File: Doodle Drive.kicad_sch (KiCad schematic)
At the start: 37 parts, among them J1 USB_B, J2 PINHD_1x4_Male, J6 PINHD_1x2_Male, SW1 Push_Button, SW2 Push_Button, SW3 Push_Button, U1 STM32F411RETx, U6 AP7343-30W5-7, U7 CP2102N-Axx-xQFN28, Y1 32.768KHz ±20ppm 12.5pF, Y2 25MHZ 9PF

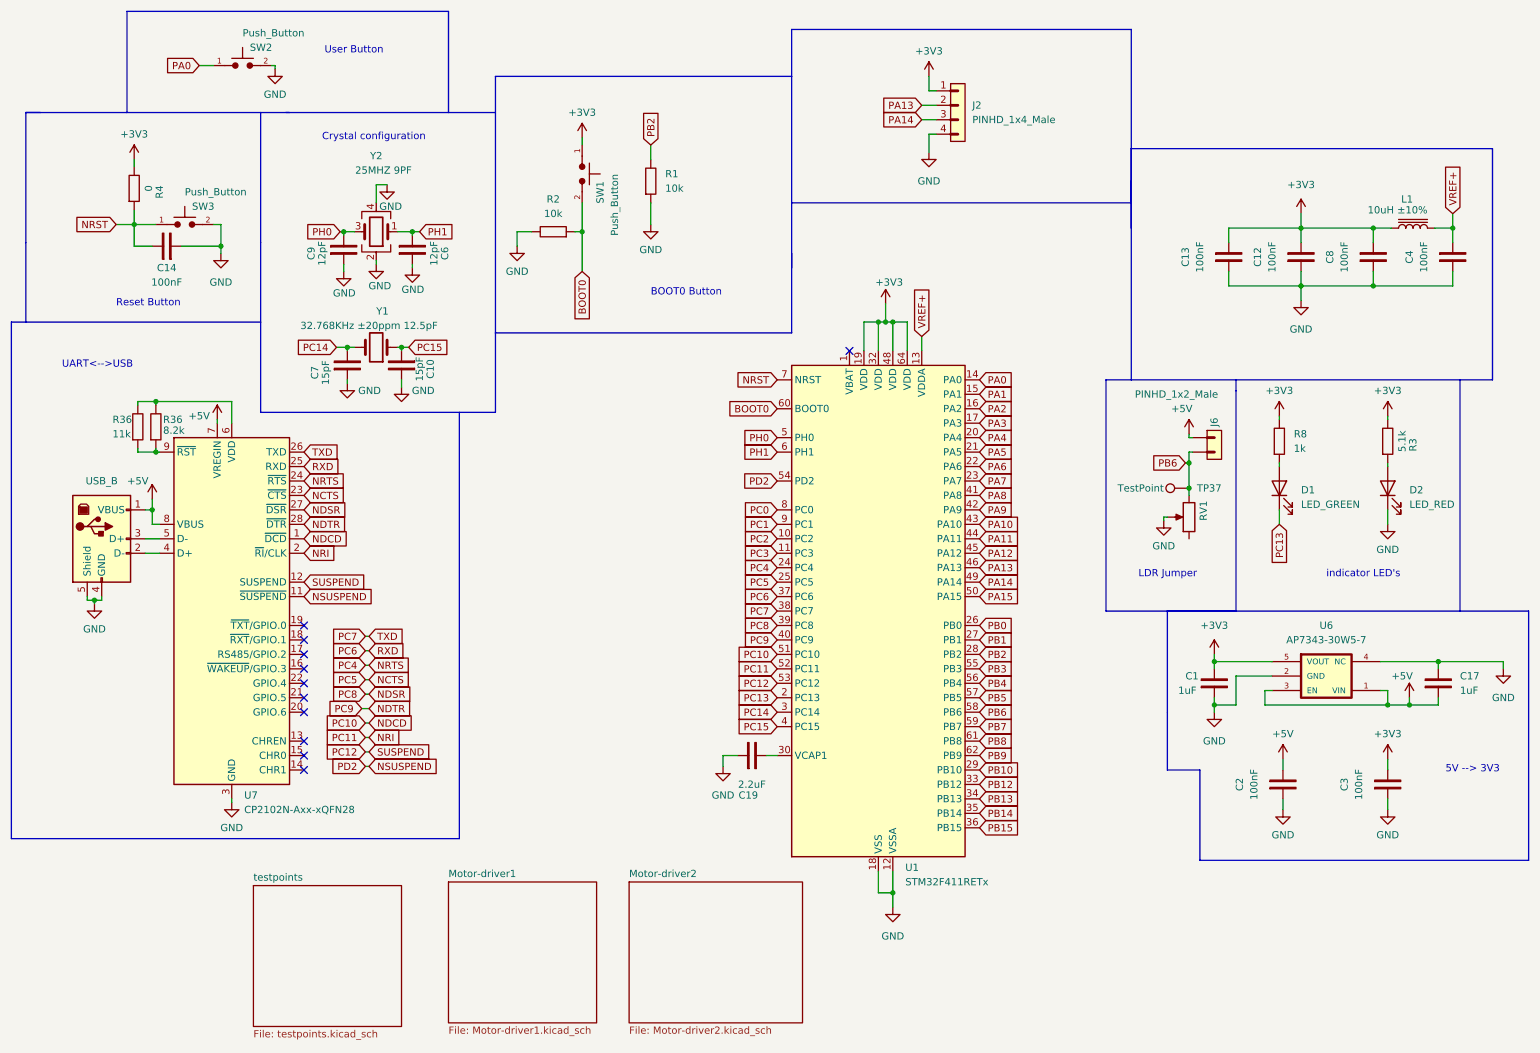
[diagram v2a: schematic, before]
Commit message: finished PCB. DRC 0 errors
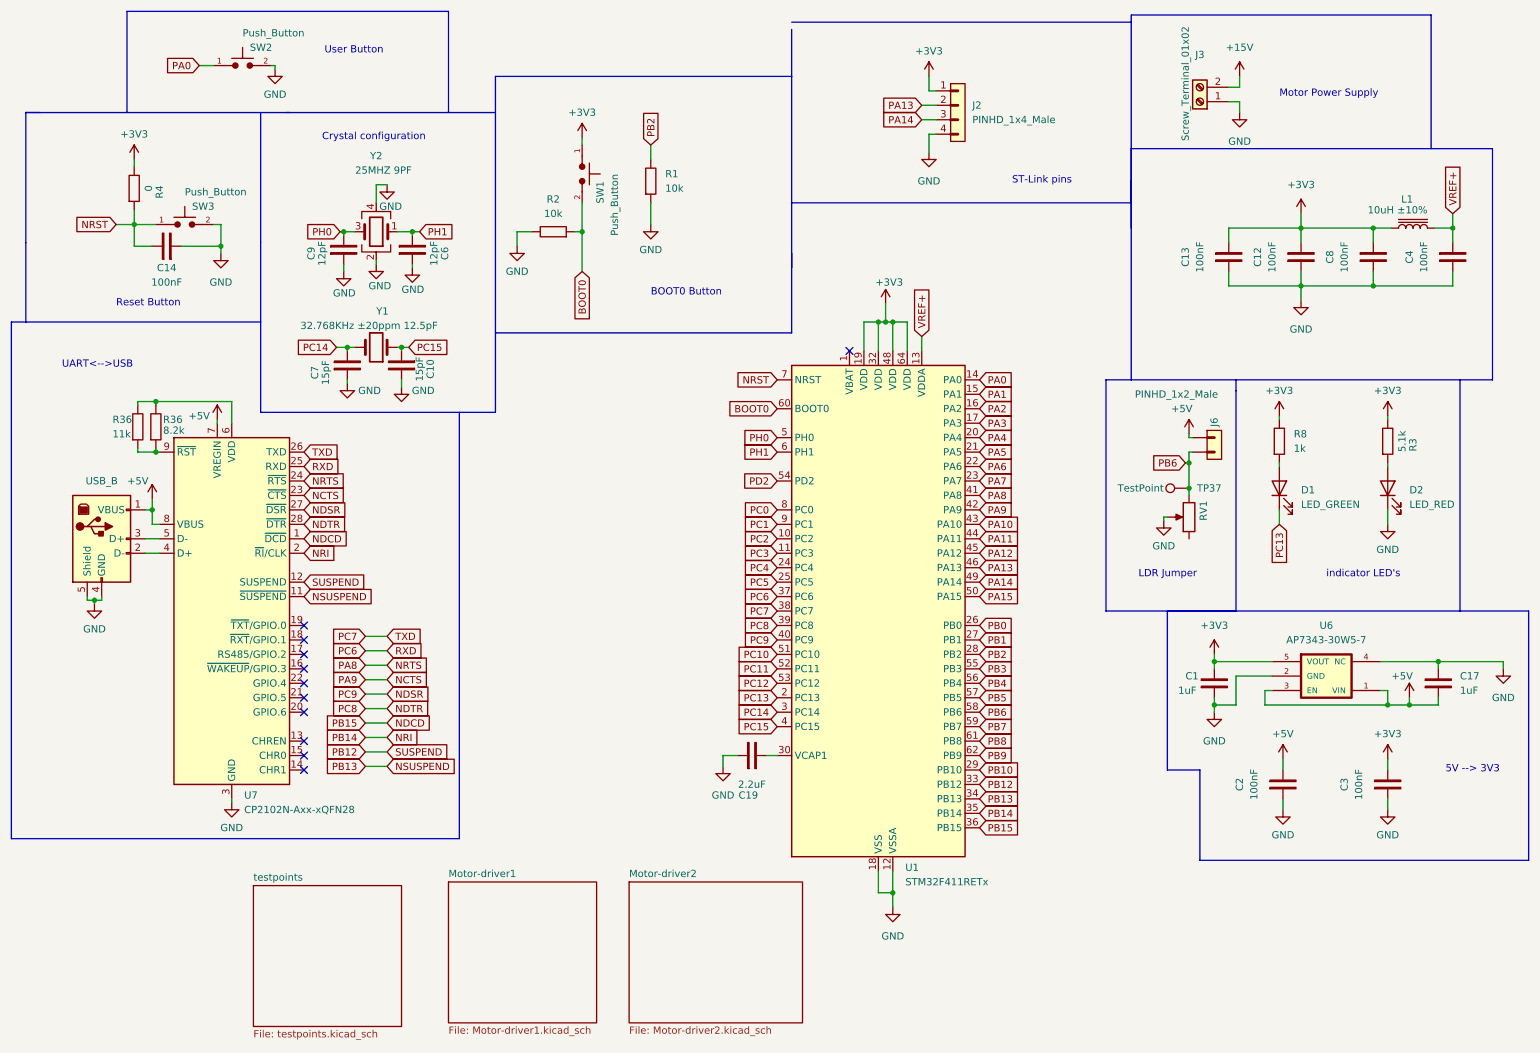
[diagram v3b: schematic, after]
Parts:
- added J3: Screw_Terminal_01x02, TerminalBlock:TerminalBlock_Altech_AK300-2_P5.00mm, symbol Connector:Screw_Terminal_01x02
- TP37: footprint TestPoint:TestPoint_Pad_D2.5mm -> TestPoint:TestPoint_Pad_D1.5mm
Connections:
- net PA8 is gone; now on net NRTS: U1.41 (PA8)
- net PA9 is gone; now on net NCTS: U1.42 (PA9)
- net PB13 is gone; now on net NSUSPEND: U1.34 (PB13)
- net PB14 is gone; now on net NRI: U1.35 (PB14)
- net PB15 is gone; now on net NDCD: U1.36 (PB15)
- net GND: now also J3.1 (Pin_1)
- net NCTS: no longer U1.25 (PC5)
- net NDCD: no longer U1.51 (PC10)
- net NDSR: now also U1.40 (PC9); no longer U1.39 (PC8)
- net NDTR: now also U1.39 (PC8); no longer U1.40 (PC9)
- net NRI: no longer U1.52 (PC11)
- net NRTS: no longer U1.24 (PC4)
- net NSUSPEND: no longer U1.54 (PD2)
- net PB12: now also U7.12 (SUSPEND)
- net PC12: no longer U7.12 (SUSPEND)
- new net +15V: J3.2 (Pin_2)
- new net PC10: U1.51 (PC10)
- new net PC11: U1.52 (PC11)
- new net PC4: U1.24 (PC4)
- new net PC5: U1.25 (PC5)
- new net PD2: U1.54 (PD2)
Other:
- note added: "Motor Power Supply"
- note added: "ST-Link pins"

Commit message: completly reroutet EVERYTHING
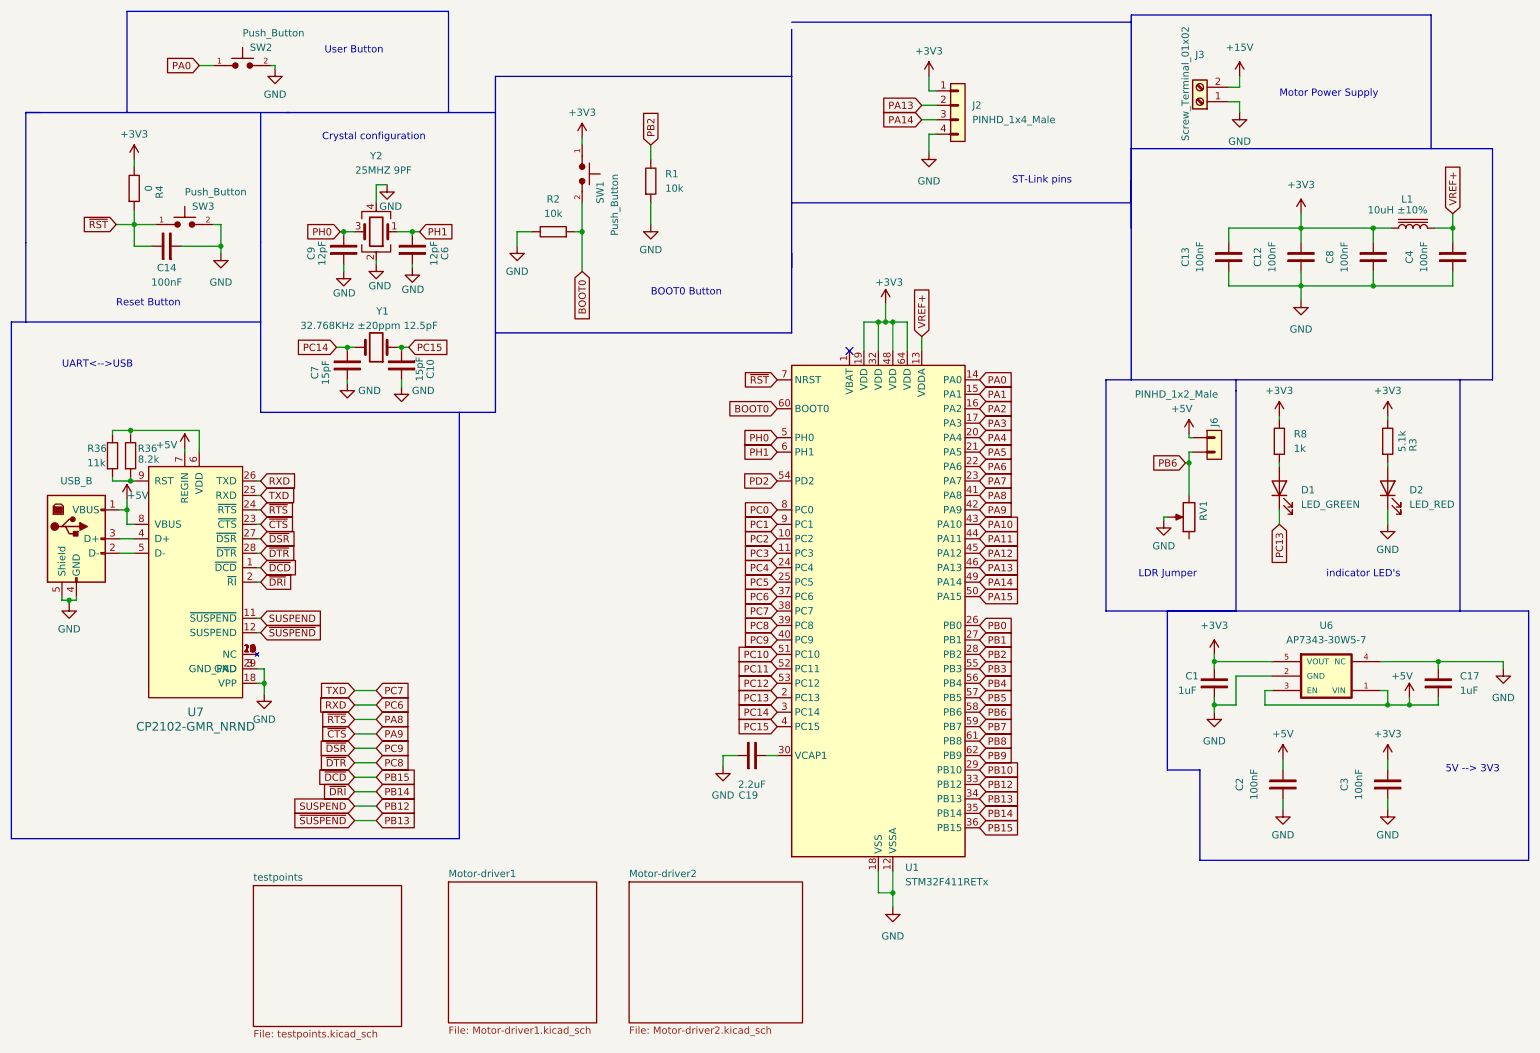
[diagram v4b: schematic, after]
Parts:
- removed TP37: TestPoint, TestPoint:TestPoint_Pad_D1.5mm, symbol Connector:TestPoint
- removed U7: CP2102N-Axx-xQFN28, Package_DFN_QFN:QFN-28-1EP_5x5mm_P0.5mm_EP3.35x3.35mm, symbol Interface_USB:CP2102N-Axx-xQFN28
- added U7: CP2102-GMR_NRND, digikey-footprints:VFQFN-28-1EP_5x5mm, symbol dk_Interface-Controllers:CP2102-GMR_NRND
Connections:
- net +5V: now also U7.7 (REGIN), U7.8 (VBUS)
- net GND: now also U7.18 (VPP), U7.29 (GND_PAD), U7.3 (GND)
- net PB12: now also U7.11 (~{SUSPEND})
- net PC6: now also U7.26 (TXD)
- net PC7: now also U7.25 (RXD)
- net at R36.1, R36.1: now also U7.9 (RST)
- net at R36.2, R36.2: now also U7.6 (VDD)
- net at J1.2 (D-): now also U7.5 (D-)
- net at J1.3 (D+): now also U7.4 (D+)
- net NCTS renamed PA9
- net PA9: now also U7.23 (~{CTS})
- net NDCD renamed PB15
- net PB15: now also U7.1 (~{DCD})
- net NDSR renamed PC9
- net PC9: now also U7.27 (~{DSR})
- net NDTR renamed PC8
- net PC8: now also U7.28 (~{DTR})
- net NRI renamed PB14
- net PB14: now also U7.2 (~{RI})
- net NRST renamed ~{RST}
- net NRTS renamed PA8
- net PA8: now also U7.24 (~{RTS})
- net NSUSPEND renamed PB13
- net PB13: now also U7.12 (SUSPEND)
- new net: U7.10 (NC), U7.13 (NC), U7.14 (NC), U7.15 (NC), U7.16 (NC), U7.17 (NC), U7.18 (VPP), U7.19 (NC), U7.20 (NC), U7.21 (NC), U7.22 (NC)
- no-connect marks 11 -> 1
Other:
- moved on the sheet: R36

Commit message: deTommaso approved version
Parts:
- removed RV1: R_Potentiometer, Potentiometer_THT:Potentiometer_ACP_CA6-H2,5_Horizontal, symbol Device:R_Potentiometer
- added RV2: R_Potentiometer, poti:3386P1473LF, symbol Device:R_Potentiometer
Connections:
- net GND: now also RV2.2
- net PB6: now also RV2.3
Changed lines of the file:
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@@
+    )
+  )
+  (symbol (lib_id "Device:R_Potentiometer") (at 222.885 101.6 180) (unit 1)
+    (in_bom yes) (on_board yes) (dnp no)
+    (property "Reference" "RV2" (at 230.505 102.87 90)
+      (effects (font (size 1.27 1.27)) (justify right))
+    )
+    (property "Value" "R_Potentiometer" (at 220.98 96.52 0)
+      (effects (font (size 1.27 1.27)) (justify right))
+    )
+    (property "Footprint" "poti:3386P1473LF" (at 222.885 101.6 0)
+      (effects (font (size 1.27 1.27)) hide)
+    )
+    (property "Datasheet" "~" (at 222.885 101.6 0)
+      (effects (font (size 1.27 1.27)) hide)
+    )
+    (pin "1")
+    (pin "2")
+    (pin "3")
+    (instances
+      (project "Doodle Drive"
+        (path "/3ec634aa-8c09-482d-9325-2288a4dbd68b/4a4951fa-be57-4d48-97a5-6be750b353b5"
+          (reference "RV2") (unit 1)
+        )
+        (path "/3ec634aa-8c09-482d-9325-2288a4dbd68b/ce40ab82-c304-4dd2-80f5-b6df1964b151"
+          (reference "RV1") (unit 1)
+        )
+        (path "/3ec634aa-8c09-482d-9325-2288a4dbd68b"
+          (reference "RV4") (unit 1)
+        )
+      )
     )
   )
@@
         )
       )
-    )
-  )
-  (symbol (lib_id "Device:R_Potentiometer") (at 222.885 101.6 180) (unit 1)
-    (in_bom yes) (on_board yes) (dnp no)
-    (property "Reference" "RV1" (at 225.425 102.235 90)
-      (effects (font (size 1.27 1.27)) (justify right))
-    )
-    (property "Value" "R_Potentiometer" (at 217.805 93.98 0)
-      (effects (font (size 1.27 1.27)) (justify right) hide)
-    )
-    (property "Footprint" "Potentiometer_THT:Potentiometer_ACP_CA6-H2,5_Horizontal" (at 222.885 101.6 0)
-      (effects (font (size 1.27 1.27)) hide)
-    )
-    (property "Datasheet" "~" (at 222.885 101.6 0)
-      (effects (font (size 1.27 1.27)) hide)
-    )
-    (pin "1")
-    (pin "2")
-    (pin "3")
-    (instances
-      (project "Doodle Drive"
-        (path "/3ec634aa-8c09-482d-9325-2288a4dbd68b/ce40ab82-c304-4dd2-80f5-b6df1964b151"
-          (reference "RV1") (unit 1)
-        )
-        (path "/3ec634aa-8c09-482d-9325-2288a4dbd68b"
-          (reference "RV5") (unit 1)
-        )
-      )

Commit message: bestellte version
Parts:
- C10, C7: footprint Capacitor_SMD:C_0805_2012Metric -> Capacitor_SMD:C_0402_1005Metric
- C6, C9: value 12pF -> 18pF
- L1: value 10uH ±10% -> 10uH
- R4: value 0 -> 0ohm
- U6: value AP7343-30W5-7 -> AP7343-33W5-7
- U7: value CP2102-GMR_NRND -> CP2102-GMR
- Y2: value 25MHZ 9PF -> 25MHZ 12PF
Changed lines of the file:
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@@
       (effects (font (size 1.27 1.27)))
     )
-    (property "Value" "12pF" (at 90.17 55.245 0)
+    (property "Value" "18pF" (at 90.17 55.245 0)
       (effects (font (size 1.27 1.27)))
     )
@@
       (effects (font (size 1.27 1.27)))
     )
-    (property "Footprint" "Capacitor_SMD:C_0805_2012Metric" (at 78.74 74.93 0)
+    (property "Footprint" "Capacitor_SMD:C_0402_1005Metric" (at 78.74 74.93 0)
       (effects (font (size 1.27 1.27)) hide)
     )
@@
       (effects (font (size 1.27 1.27)))
     )
-    (property "Value" "AP7343-30W5-7" (at 247.015 123.19 0)
+    (property "Value" "AP7343-33W5-7" (at 247.015 123.19 0)
       (effects (font (size 1.27 1.27)))
     )
@@
       (effects (font (size 1.27 1.27)))
     )
-    (property "Value" "12pF" (at 70.485 55.245 0)
+    (property "Value" "18pF" (at 70.485 55.245 0)
       (effects (font (size 1.27 1.27)))
     )
@@
       (effects (font (size 1.27 1.27)))
     )
-    (property "Value" "0" (at 40.005 43.815 0)
+    (property "Value" "0ohm" (at 40.005 43.815 0)
       (effects (font (size 1.27 1.27)))
     )
@@
       (effects (font (size 1.27 1.27)) (justify left))
     )
-    (property "Value" "10uH ±10%" (at 264.795 47.625 90)
+    (property "Value" "10uH" (at 264.795 47.625 90)
       (effects (font (size 1.27 1.27)) (justify left))
     )
@@
       (effects (font (size 1.524 1.524)))
     )
-    (property "Value" "CP2102-GMR_NRND" (at 48.26 138.43 0)
+    (property "Value" "CP2102-GMR" (at 48.26 138.43 0)
       (effects (font (size 1.524 1.524)))
     )
@@
       (effects (font (size 1.27 1.27)))
     )
-    (property "Footprint" "Capacitor_SMD:C_0805_2012Metric" (at 80.645 74.93 0)
+    (property "Footprint" "Capacitor_SMD:C_0402_1005Metric" (at 80.645 74.93 0)
       (effects (font (size 1.27 1.27)) hide)
     )
@@
       (effects (font (size 1.27 1.27)))
     )
-    (property "Value" "25MHZ 9PF" (at 81.28 40.64 0)
-      (effects (font (size 1.27 1.27)))
-    )
+    (property "Value" "25MHZ 12PF" (at 81.28 40.64 0)
+      (effects (font (size 1.27 1.27)))
+    )
